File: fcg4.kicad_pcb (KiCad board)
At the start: 4 copper layers, 34 x 34 mm, 107 parts, among them IC1 MP9943AGQ-Z, IC2 MP9943AGQ-Z, J1 USB4105-GF-A-120, J2 SM08B-SRSS-TB, U1 STM32G473CEUx, U10 MAX40200ANS_T, U11 MAX40200ANS_T, U2 ICM-42688-P, U23 SDA, U26 SCL, U31 9V, U4 AP2112K-3.3TRG1, U5 AP2112K-1.8TRG1, Y1 ECS-240-6-37B-7KM-TR

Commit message: routing...
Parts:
- moved J2 1.32 mm to (23.4, -0.30)
- moved U18 1.21 mm to (0.90, 14.7)
- moved U19 1.21 mm to (0.90, 12.5)
- moved U22 0.73 mm to (0.90, 23.8)
- moved U24 0.73 mm to (0.90, 25.8)
- moved U25 0.73 mm to (0.90, 27.8)
- moved J1 0.60 mm to (31.7, 21.6)
- moved U28 0.51 mm to (17.7, 33.1)
- moved U9 0.51 mm to (17.7, 29.9)
- moved U23 0.51 mm to (13.3, 29.9)
- moved U26 0.51 mm to (15.5, 29.9)
- moved U27 0.51 mm to (6.70, 33.1)
- moved U29 0.51 mm to (11.1, 33.1)
- moved U30 0.51 mm to (13.3, 33.1)
- moved U31 0.51 mm to (15.5, 33.1)
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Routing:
- net TX3: track 29.6 -> 52.5 mm
- net /Connectors/MOTOR_3: track 20.2 -> 5.28 mm, vias 2 -> 1
- net /Connectors/MOTOR_4: track 21.0 -> 7.23 mm, vias 2 -> 1
- net /Connectors/MOTOR_1: track 24.8 -> 18.2 mm, vias 2 -> 1
- net /Connectors/MOTOR_2: track 25.0 -> 23.9 mm, vias 2 -> 1
- net 5V_USB: track 5.19 -> 5.79 mm
- net /MCU/USB_DIFF+: track 8.69 -> 8.19 mm
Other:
- board size 34 x 34 mm -> 35 x 35 mm

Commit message: update edges
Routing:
- net TX3: track 52.5 -> 30.1 mm
- net /Connectors/MOTOR_3: track 5.28 -> 22.0 mm, vias 1 -> 2
- net /Connectors/MOTOR_4: track 7.23 -> 23.2 mm, vias 1 -> 2
- net /Connectors/MOTOR_1: track 18.2 -> 26.0 mm, vias 1 -> 2
- net /Connectors/MOTOR_2: track 23.9 -> 26.4 mm, vias 1 -> 2
- net RX2: track 20.5 -> 21.9 mm
- net CURRENT_SENSOR: track 20.3 -> 21.6 mm
- net RX3: track 53.5 -> 54.6 mm
- net RX4: track 30.2 -> 30.8 mm
- net BZ: track 24.5 -> 25.2 mm
- net GND: track 65.4 -> 66.0 mm, vias 40 -> 41
- net I2C1_SDA: track 26.8 -> 27.4 mm
- net 9V_BEC: track 37.4 -> 37.9 mm
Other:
- outline, holes or cut-outs redrawn

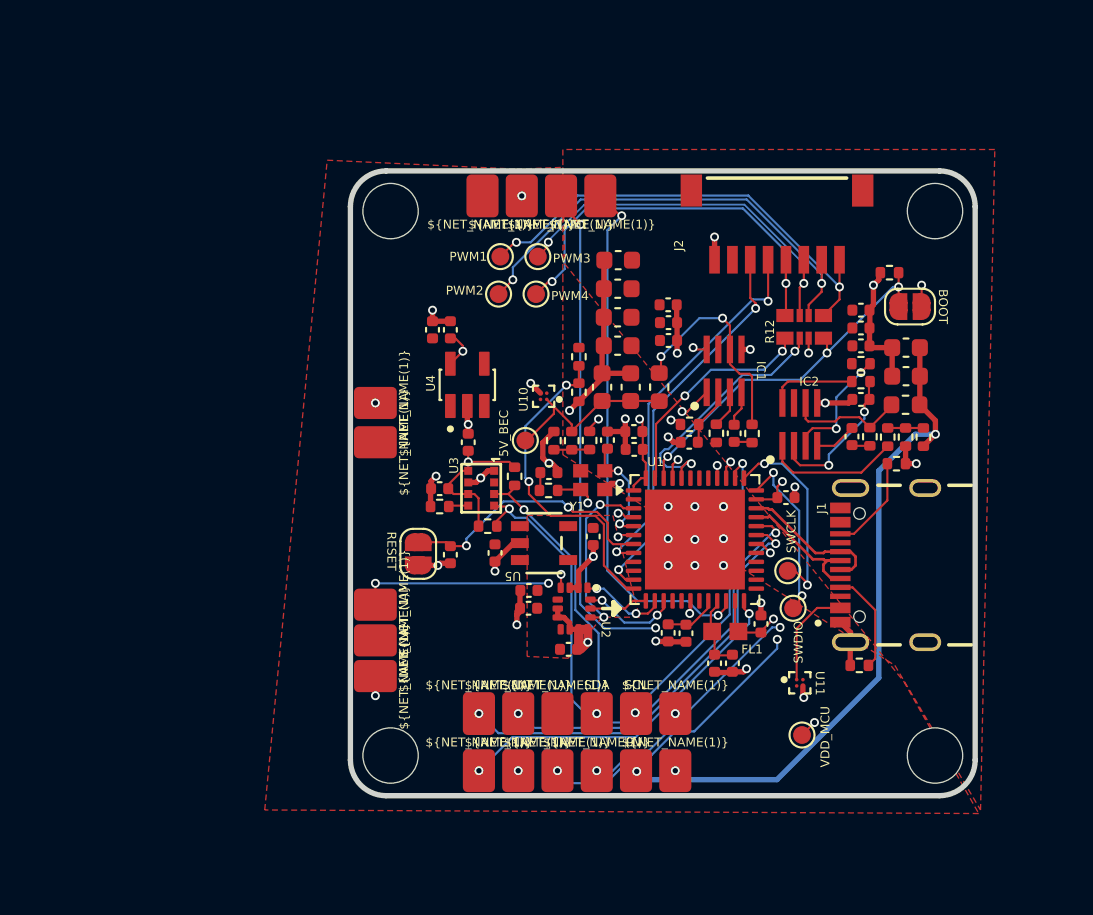
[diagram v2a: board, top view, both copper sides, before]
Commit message: Almost completed! Update component properties in sensor schematic
- Added datasheets, LCSC part names, manufacturer names, and manufacturer part numbers for various components in the sensor.kicad_sch file.
- Updated the datasheet links for components to point to the correct URLs.
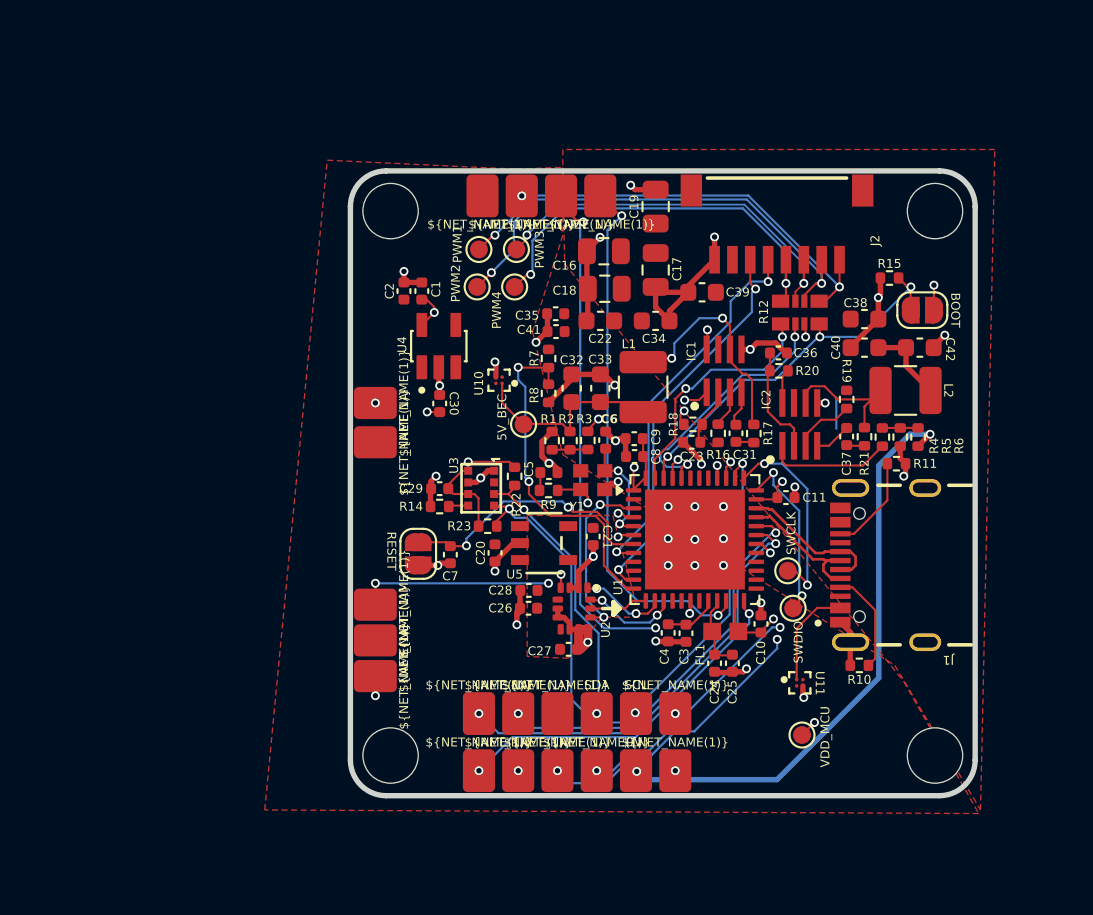
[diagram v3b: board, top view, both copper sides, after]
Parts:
- C16, C17, C18, C19: footprint Capacitor_SMD:C_0603_1608Metric -> Capacitor_SMD:C_0805_2012Metric
- C22, C34, C38, C39: footprint Capacitor_SMD:C_0402_1005Metric -> Capacitor_SMD:C_0603_1608Metric
- L1, L2: footprint Inductor_SMD:L_0603_1608Metric -> Inductor_SMD:L_1210_3225Metric
- R9: value 250 -> 249
- moved C41 17.1 mm to (11.0, 8.50), turned to 0 degrees
- moved C39 9.39 mm to (19.2, 6.30), turned to 0 degrees
- moved C35 6.50 mm to (11.0, 7.50), turned to 0 degrees
- moved C36 5.30 mm to (23.5, 9.70), turned to 0 degrees
- moved R20 4.64 mm to (23.5, 10.7), turned to 180 degrees
- moved C22 3.82 mm to (13.5, 7.90), turned to 0 degrees
- moved C19 3.66 mm to (16.6, 1.50), turned to 90 degrees
- moved C17 3.40 mm to (16.6, 5.05), turned to -90 degrees
- moved C18 3.27 mm to (13.8, 6.10)
- moved C40 2.82 mm to (28.3, 9.40)
- moved C1 2.70 mm to (3.50, 6.23)
- moved C2 2.70 mm to (2.50, 6.23)
- moved C30 2.70 mm to (4.50, 12.5)
- moved U4 2.70 mm to (4.45, 9.31)
- moved U10 2.66 mm to (7.83, 11.2)
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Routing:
- net GND: track 66.0 -> 74.5 mm, vias 41 -> 44
- net /Power/PG_9V: track 5.19 -> 1.93 mm
- net /Power/BIAS_SUPPLY_9V: track 8.50 -> 6.17 mm, vias 2 -> 0
- net /Power/EN/SYNC_9V: track 6.92 -> 5.28 mm, vias 2 -> 0
- net VOLTAGE_SENSOR: track 18.3 -> 19.6 mm
- net /Power/LC_9V: track 6.67 -> 7.92 mm
- net MOTOR4: track 12.6 -> 13.7 mm
- net /Connectors/MOTOR_2: track 26.4 -> 27.4 mm
- net 5V5_BEC: track 10.6 -> 11.5 mm
- net MOTOR1: track 21.0 -> 21.9 mm
- net MOTOR2: track 24.7 -> 25.6 mm
- net 9V_BEC: track 37.9 -> 37.1 mm
- net /Power/FB_9V: track 7.66 -> 7.03 mm
- net /Power/PG_5V5: track 6.47 -> 7.04 mm
- net /Connectors/MOTOR_1: track 26.0 -> 26.6 mm
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
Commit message: PCB v1 ready for manufacturing all the CAM files are available in CAM folder
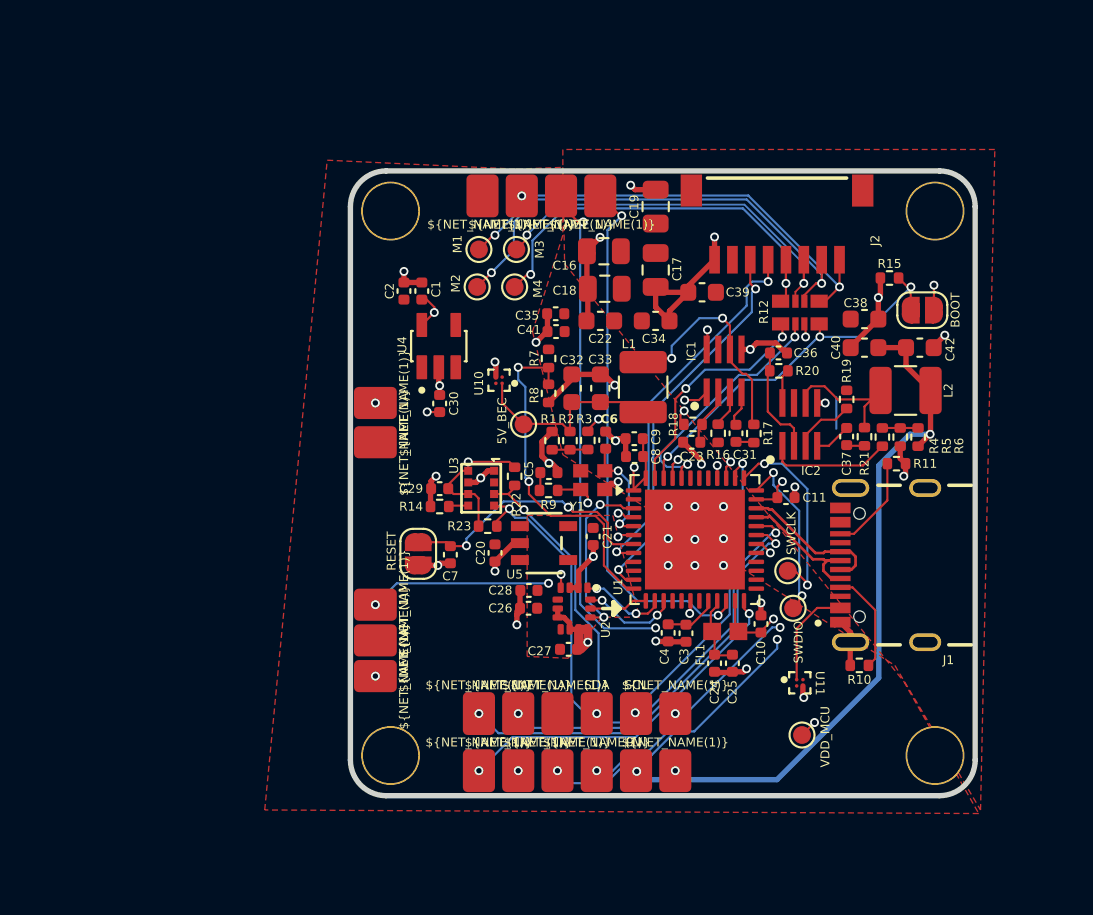
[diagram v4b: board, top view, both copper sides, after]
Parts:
- TP4: value PWM1 -> M1
- TP5: value PWM2 -> M2
- TP6: value PWM3 -> M3
- TP7: value PWM4 -> M4
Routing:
- net 9V_BEC: track 37.1 -> 39.5 mm
- net GND: track 74.5 -> 73.2 mm
- net BZ: track 25.2 -> 24.3 mm

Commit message: Add Availability and Price properties to multiple components in schematic
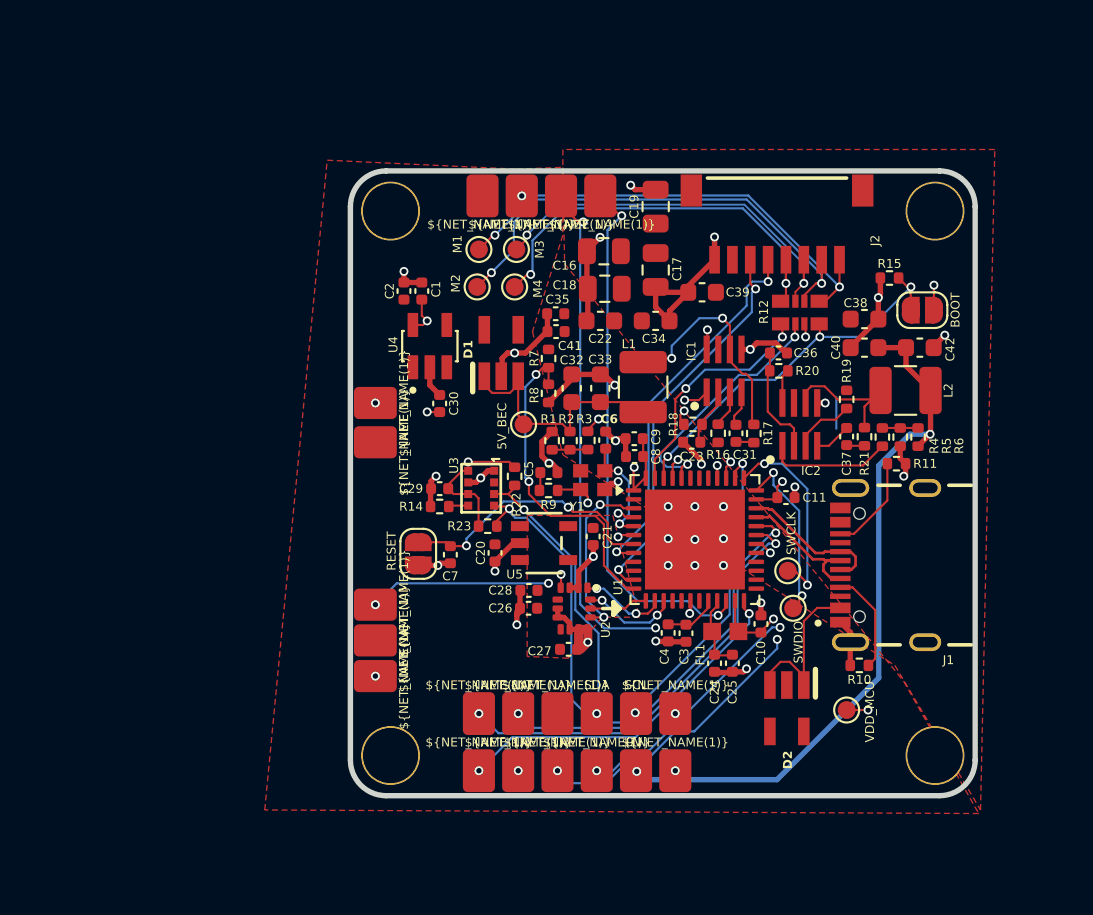
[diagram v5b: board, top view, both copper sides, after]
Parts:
- removed U10, U11: MAX40200ANS_T, fcg4_fp:BGA4N35P2X2_72X72X50N
- added D1: MAX40203AUK+T, fcg4_fp:SOT95P280X145-5M, F.Cu at (7.95, 9.70)
- added D2: MAX40203AUK+T, fcg4_fp:SOT95P280X145-5M, F.Cu at (23.9, 29.6)
- moved TP3 2.87 mm to (27.3, 29.7)
- moved U4 0.50 mm to (3.95, 9.31)
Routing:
- net 5V_USB: track 5.79 -> 9.61 mm
- net 5V5_BEC: track 11.5 -> 14.8 mm
- net GND: track 73.2 -> 75.1 mm, vias 44 -> 41
- net VOLTAGE_SENSOR: track 19.6 -> 18.4 mm

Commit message: update buck regulator to a more recent one
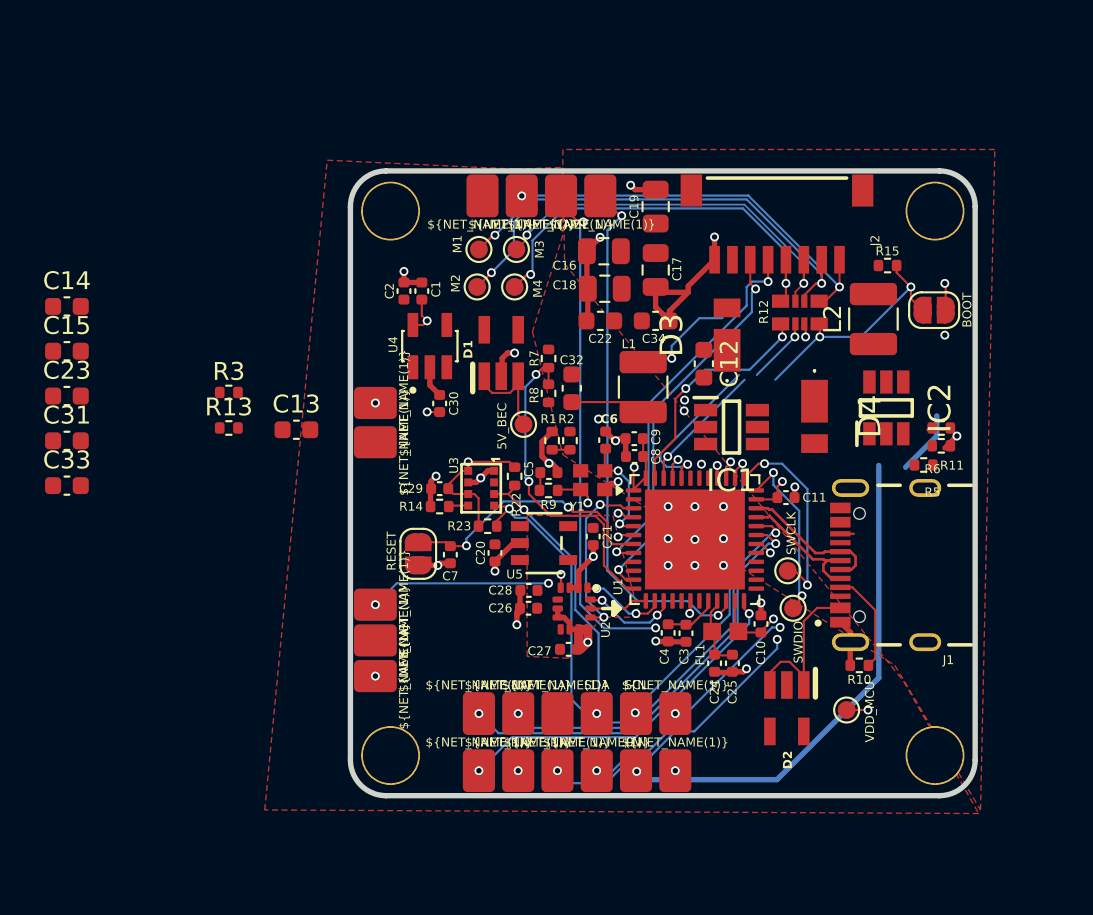
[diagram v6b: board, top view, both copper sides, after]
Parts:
- removed C35, C41: 1u, Capacitor_SMD:C_0402_1005Metric
- removed C36, C37: 100n, Capacitor_SMD:C_0402_1005Metric
- removed C38, C39: 10u, Capacitor_SMD:C_0603_1608Metric
- removed C40, C42: 22u, Capacitor_SMD:C_0603_1608Metric
- removed R16, R19: 1M, Resistor_SMD:R_0402_1005Metric
- removed R17, R21: 20, Resistor_SMD:R_0402_1005Metric
- removed R18, R20: 100k, Resistor_SMD:R_0402_1005Metric
- removed R4: 51k, Resistor_SMD:R_0402_1005Metric
- added C12: 100n, Capacitor_SMD:C_0603_1608Metric, F.Cu at (19.3, 10.3)
- added C13: 47p, Capacitor_SMD:C_0603_1608Metric, F.Cu at (-3.52, 14.0)
- added C14: 47p, Capacitor_SMD:C_0603_1608Metric, F.Cu at (-16.4, 7.09)
- added C15: 100n, Capacitor_SMD:C_0603_1608Metric, F.Cu at (-16.4, 9.60)
- added D3: DFLS160-7, fcg4_fp:DFLS1607, F.Cu at (20.6, 8.70)
- added D4: DFLS160-7, fcg4_fp:DFLS1607, F.Cu at (25.5, 13.2)
- added R13: 500k, Resistor_SMD:R_0402_1005Metric, F.Cu at (-7.31, 13.9)
- C22: value 10u -> 4.7u
- C23: value 100n -> 4.7u; footprint Capacitor_SMD:C_0402_1005Metric -> Capacitor_SMD:C_0603_1608Metric
- C31: value 100n -> 0.1u; footprint Capacitor_SMD:C_0402_1005Metric -> Capacitor_SMD:C_0603_1608Metric
- C32, C33: value 22u -> 10u
- C34: value 10u -> 0.1u
- IC1, IC2: value MP9943AGQ-Z -> MP2456GJ-Z; footprint fcg4_fp:SON65P300X300X100-8M -> fcg4_fp:SOP95P280X100-6M
- R1: value 7.68k -> 23k
- R2, R6: value 41.2k -> 124k
- R3: value 51k -> 500k
- R5: value 3.92k -> 11k
- moved C31 37.5 mm to (-16.4, 14.6), turned to 0 degrees
- moved C23 35.1 mm to (-16.4, 12.1), turned to 0 degrees
- moved C33 30.4 mm to (-16.4, 17.1), turned to 0 degrees
- moved R3 20.3 mm to (-7.31, 11.9), turned to 0 degrees
- moved IC2 4.94 mm to (29.5, 12.8)
- moved L2 4.39 mm to (28.8, 7.80), turned to 90 degrees
- moved IC1 3.18 mm to (20.9, 13.8), turned to 0 degrees
- moved R5 2.35 mm to (32.6, 14.9), turned to 180 degrees
- moved R11 1.53 mm to (31.6, 16.0)
- moved R6 1.40 mm to (32.6, 13.9), turned to 180 degrees
- moved R15 0.71 mm to (29.6, 4.80)
- moved JP2 0.66 mm to (32.2, 7.30)
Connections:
- net /Power/LC_5V5 renamed /Power/SW_5V5
- net /Power/LC_9V renamed /Power/SW_9V
- C23 pad 1: /Power/BIAS_SUPPLY_5V5 -> GND
- C23 pad 2: GND -> VBAT
- C31 pad 1: /Power/BST_5V5 -> GND
- C31 pad 2: /Power/RC_BST_5V5 -> VBAT
- C33 pad 2: 5V5_BEC -> 9V_BEC
- IC1 pad 1: /Power/FB_5V5 -> /Power/BST_5V5
- IC1 pad 2: /Power/BIAS_SUPPLY_5V5 -> GND
- IC1 pad 3: /Power/EN/SYNC_5V5 -> /Power/FB_5V5
- IC1 pad 4: /Power/BST_5V5 -> Net-(IC1-EN)
- IC1 pad 5: GND -> VBAT
- IC2 pad 1: /Power/FB_9V -> /Power/BST_9V
- IC2 pad 2: /Power/BIAS_SUPPLY_9V -> GND
- IC2 pad 3: /Power/EN/SYNC_9V -> /Power/FB_9V
- IC2 pad 4: /Power/BST_9V -> Net-(IC2-EN)
- IC2 pad 5: GND -> VBAT
- R1 pad 1: Net-(R1-Pad1) -> /Power/FB_5V5
- R2 pad 1: Net-(R1-Pad1) -> /Power/FB_5V5
- R2 pad 2: 5V5_BEC -> Net-(C13-Pad2)
- R3 pad 1: /Power/FB_5V5 -> VBAT
- R3 pad 2: Net-(R1-Pad1) -> Net-(IC2-EN)
- R5 pad 1: Net-(R4-Pad2) -> /Power/FB_9V
- R6 pad 1: Net-(R4-Pad2) -> /Power/FB_9V
- R6 pad 2: 9V_BEC -> Net-(C14-Pad2)
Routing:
- net GND: track 75.1 -> 54.3 mm, vias 41 -> 36
- net 9V_BEC: track 39.5 -> 28.2 mm, vias 2 -> 1
- net /Power/SW_9V: track 7.92 -> 0.00 mm
- net /Power/PG_5V5: track 7.04 -> 0.00 mm, vias 2 -> 0
- net /Power/SW_5V5: track 12.6 -> 5.88 mm, vias 2 -> 1
- net /Power/BIAS_SUPPLY_9V: track 6.17 -> 0.00 mm
- net /Power/EN/SYNC_9V: track 5.28 -> 0.00 mm
- net (no net): track 0.00 -> 5.08 mm, vias 0 -> 1
- net /Power/FB_9V: track 7.03 -> 1.98 mm, vias 0 -> 1
- net /MCU/CC2: track 5.47 -> 0.76 mm
- net 5V5_BEC: track 14.8 -> 10.5 mm
- net /Power/BIAS_SUPPLY_5V5: track 4.09 -> 0.00 mm
- net Net-(C14-Pad2): track 0.00 -> 3.60 mm
- net /Power/EN/SYNC_5V5: track 2.10 -> 0.00 mm
- net /Power/BST_9V: track 2.06 -> 0.00 mm
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
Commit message: finished re routing with new buck regulators
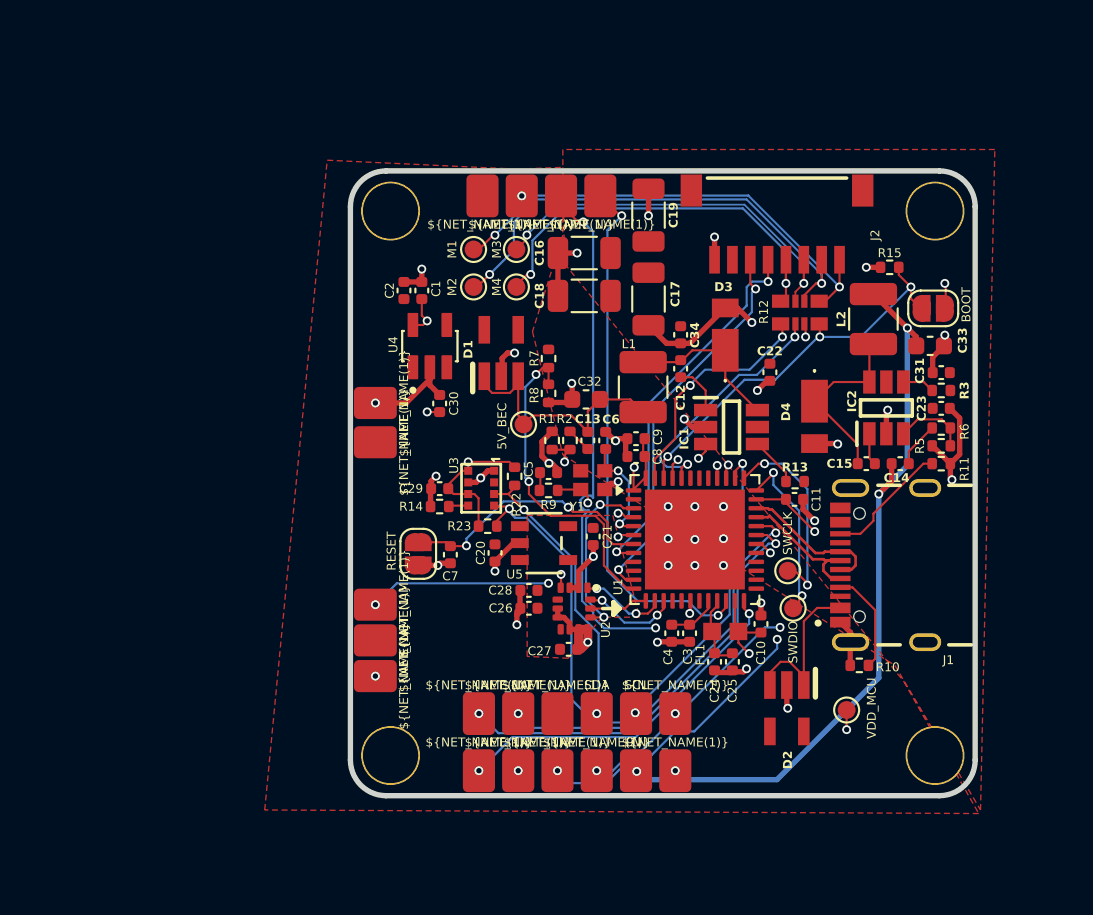
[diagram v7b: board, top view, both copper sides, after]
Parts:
- C12, C13, C14, C15, C22, C23: footprint Capacitor_SMD:C_0603_1608Metric -> Capacitor_SMD:C_0402_1005Metric
- C16, C17, C18, C19: footprint Capacitor_SMD:C_0805_2012Metric -> Capacitor_SMD:C_1206_3216Metric
- C31, C34: value 0.1u -> 100n; footprint Capacitor_SMD:C_0603_1608Metric -> Capacitor_SMD:C_0402_1005Metric
- moved C31 49.1 mm to (32.6, 10.8)
- moved C23 49.0 mm to (32.6, 12.8), turned to 180 degrees
- moved C33 49.0 mm to (32.0, 9.30), turned to 180 degrees
- moved C14 47.5 mm to (30.3, 15.9)
- moved C15 45.2 mm to (28.4, 15.9)
- moved R3 39.9 mm to (32.6, 11.8), turned to 180 degrees
- moved R13 31.9 mm to (24.4, 16.9), turned to 180 degrees
- moved C13 16.3 mm to (12.8, 14.6), turned to -90 degrees
- moved C22 9.93 mm to (23.0, 10.8), turned to 90 degrees
- moved C17 1.67 mm to (16.2, 6.67)
- moved C34 1.60 mm to (18.0, 8.68), turned to 90 degrees
- moved C12 1.33 mm to (18.0, 10.6)
- moved C18 1.22 mm to (12.6, 6.50)
- moved C16 1.10 mm to (12.6, 4.10)
- moved C32 1.02 mm to (12.7, 12.3), turned to 0 degrees
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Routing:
- net GND: track 54.3 -> 73.9 mm, vias 36 -> 44
- net 9V_BEC: track 28.2 -> 42.4 mm, vias 1 -> 3
- net /Power/SW_9V: track 0.00 -> 10.2 mm
- net /MCU/CC2: track 0.76 -> 7.01 mm
- net (no net): track 5.08 -> 0.00 mm, vias 1 -> 0
- net 5V5_BEC: track 10.5 -> 15.1 mm
- net /Power/FB_5V5: track 6.28 -> 10.8 mm
- net /Power/SW_5V5: track 5.88 -> 9.27 mm, vias 1 -> 0
- net /Power/BST_5V5: track 0.00 -> 2.81 mm
- net Net-(IC1-EN): track 0.00 -> 2.76 mm
- net VDD_MCU: track 25.2 -> 27.4 mm
- net /Power/FB_9V: track 1.98 -> 4.17 mm, vias 1 -> 0
- net Net-(IC2-EN): track 0.00 -> 1.81 mm
- net /Power/BST_9V: track 0.00 -> 1.80 mm
- net MOTOR1: track 21.3 -> 22.9 mm
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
